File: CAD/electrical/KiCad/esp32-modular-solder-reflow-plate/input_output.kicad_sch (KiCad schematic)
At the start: 66 parts, among them J5 Heater, J6 PWR_IN, Q3 BUZ_CTL

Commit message: - cad: add an auxiliary temperature probe input
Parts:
- added J5: Thermo Coupler, Connector_JST:JST_XH_B2B-XH-A_1x02_P2.50mm_Vertical, symbol Connector_Generic:Conn_01x02
- J4: renamed from J?; value Thermo Coupler -> Aux Thermo Coupler
- gave numbers to parts that had none: 58
- renumbered C27 to C30, J5 to J6, J6 to J7
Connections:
- new net AUX_THCPL_n: J5.1 (Pin_1)
- new net AUX_THCPL_p: J5.2 (Pin_2)
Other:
- moved on the sheet: J4, J6, J7

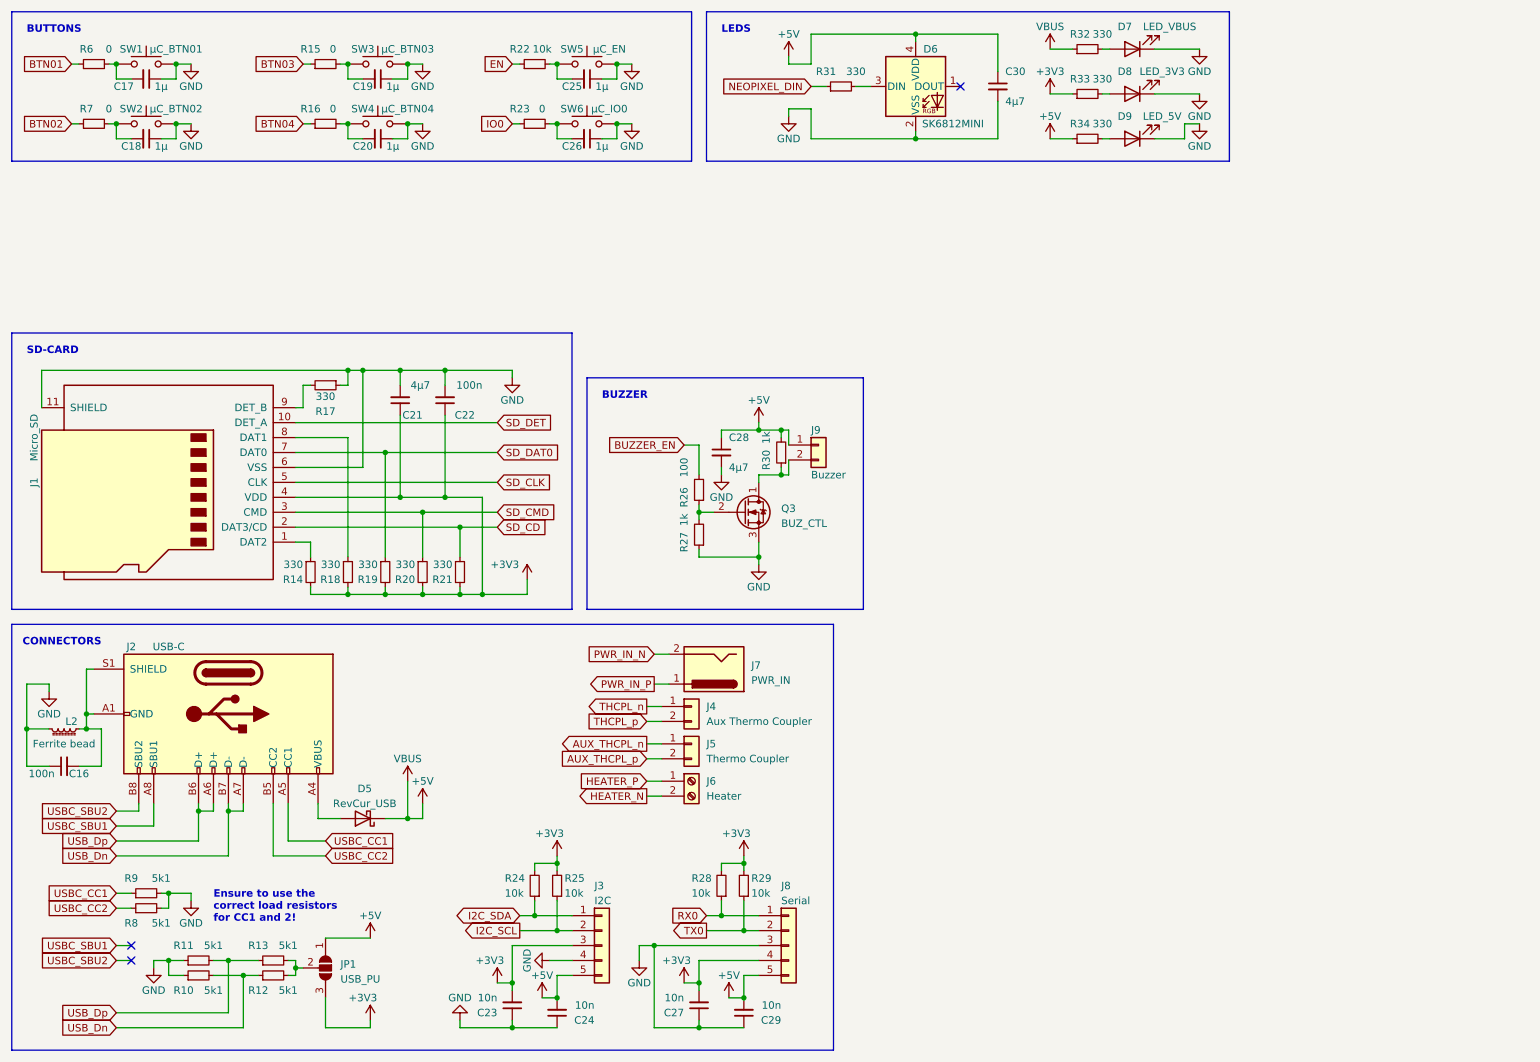
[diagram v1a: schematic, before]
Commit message: - CAD: added usb pd trigger configurable via esp, routing adjustments
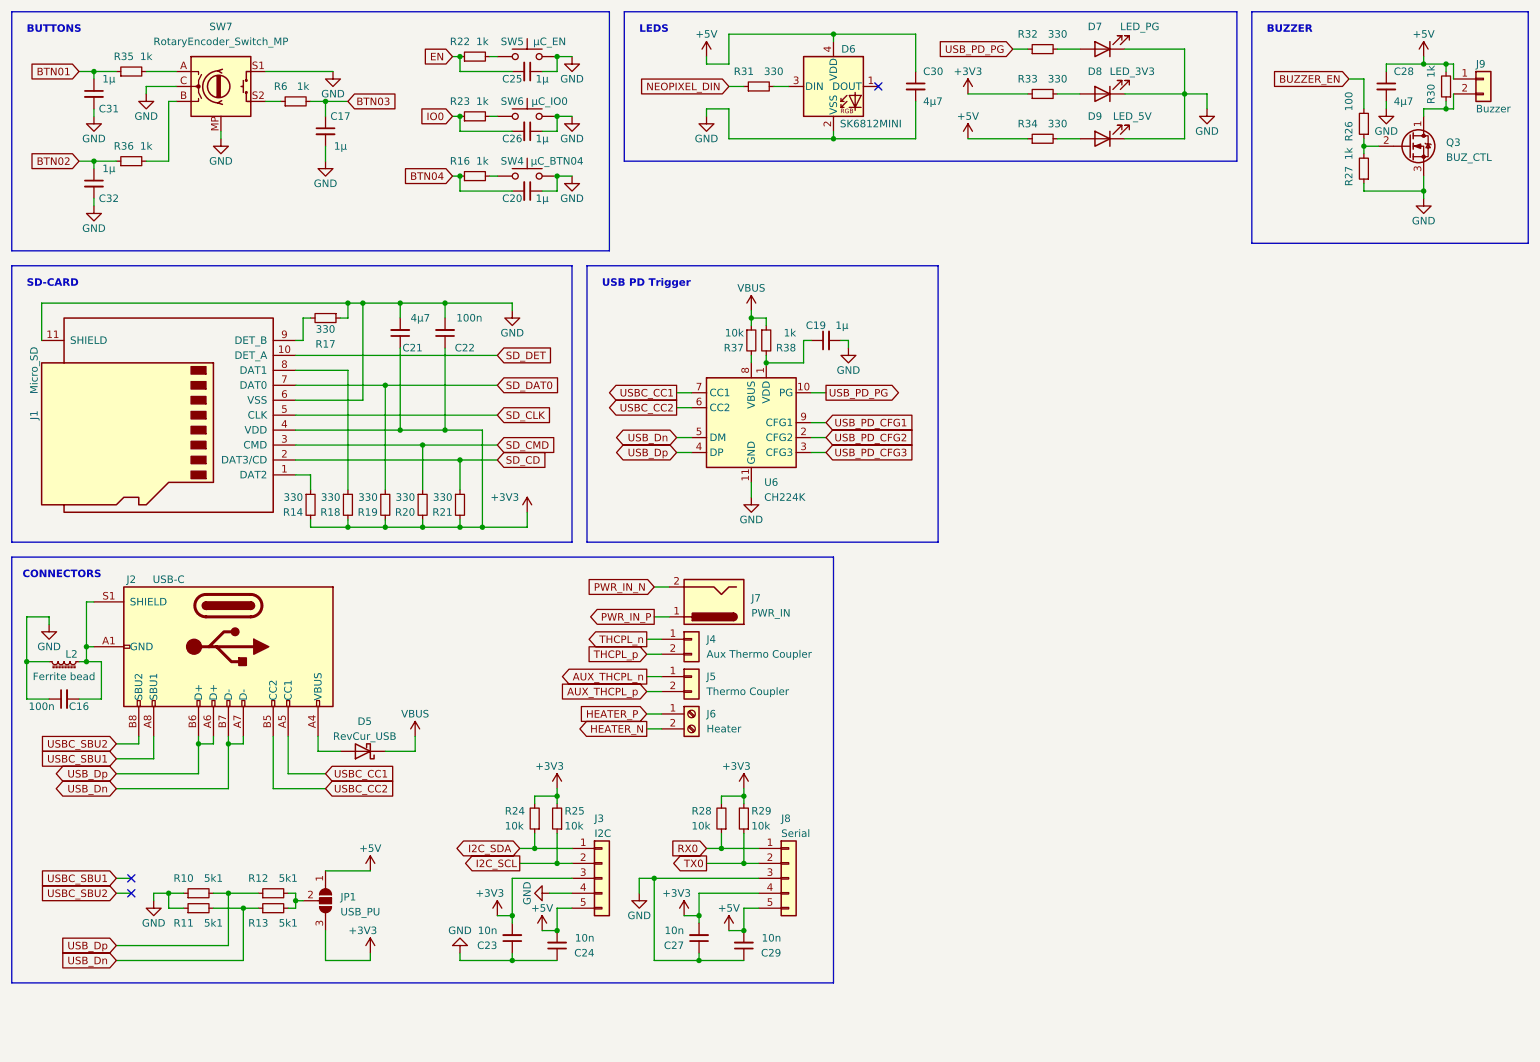
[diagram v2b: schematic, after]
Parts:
- removed C18: 1µ, Capacitor_SMD:C_0603_1608Metric_Pad1.08x0.95mm_HandSolder, symbol Device:C_Small
- removed R15, R7: 0, Resistor_SMD:R_0603_1608Metric_Pad0.98x0.95mm_HandSolder, symbol Device:R_Small
- removed R8, R9: 5k1, Resistor_SMD:R_0603_1608Metric_Pad0.98x0.95mm_HandSolder, symbol Device:R_Small
- removed SW1: µC_BTN01, Button_Switch_THT:SW_PUSH_6mm, symbol Switch:SW_Push
- removed SW2: µC_BTN02, Button_Switch_THT:SW_PUSH_6mm, symbol Switch:SW_Push
- removed SW3: µC_BTN03, Button_Switch_THT:SW_PUSH_6mm, symbol Switch:SW_Push
- added C31, C32: 1µ, Capacitor_SMD:C_0603_1608Metric_Pad1.08x0.95mm_HandSolder, symbol Device:C_Small
- added R35, R36, R38: 1k, Resistor_SMD:R_0603_1608Metric_Pad0.98x0.95mm_HandSolder, symbol Device:R_Small
- added R37: 10k, Resistor_SMD:R_0603_1608Metric_Pad0.98x0.95mm_HandSolder, symbol Device:R_Small
- added SW7: RotaryEncoder_Switch_MP, Rotary_Encoder:RotaryEncoder_Alps_EC11E-Switch_Vertical_H20mm, symbol Device:RotaryEncoder_Switch_MP
- added U6: CH224K, Package_SO:SSOP-10-1EP_3.9x4.9mm_P1mm_EP2.1x3.3mm, symbol Interface_USB:CH224K
- D7: value LED_VBUS -> LED_PG
- J2: footprint Connector_USB:USB_C_Receptacle_GCT_USB4085 -> Connector_USB:USB_C_Receptacle_G-Switch_GT-USB-7010ASV
- R16, R23, R6: value 0 -> 1k
- R22: value 10k -> 1k
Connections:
- net +5V: no longer D5.1 (K), R32.1
- net BTN01: now also C31.1, R35.1; no longer R6.1
- net BTN02: now also C32.1, R36.1
- net BTN03: now also C17.1, R6.2
- net BTN04: now also C20.2
- net EN: now also C25.2
- net GND: now also C17.2, C19.2, C31.2, C32.2, SW7.C, SW7.MP, SW7.S1, U6.11 (GND); no longer C17.1, C19.1
- net IO0: now also C26.2
- net USBC_CC1: now also U6.7 (CC1)
- net USBC_CC2: now also U6.6 (CC2)
- net USB_Dn: now also U6.5 (DM)
- net USB_Dp: now also U6.4 (DP)
- net at R16.2, SW4.1: no longer C20.2
- net at R22.2, SW5.1: no longer C25.2
- net at R23.2, SW6.1: no longer C26.2
- new net: R6.1, SW7.S2
- new net: R35.2, SW7.A
- new net: R36.2, SW7.B
- new net: C19.1, R38.2, U6.1 (VDD)
- new net: R37.2, U6.8 (VBUS)
- new net USB_PD_CFG1: U6.9 (CFG1)
- new net USB_PD_CFG2: U6.2 (CFG2)
- new net USB_PD_CFG3: U6.3 (CFG3)
- new net USB_PD_PG: R32.1, U6.10 (PG)
- new net VBUS: D5.1 (K), R37.1, R38.1
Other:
- note added: "USB PD Trigger"
- note removed: "Ensure to use the correct load resistors for CC1 and 2!"
- moved on the sheet: C16, C20, C21, C22, C23, C24, C25, C26, C27, C28, C29, C30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
